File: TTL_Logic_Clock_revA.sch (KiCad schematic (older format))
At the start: 93 parts, among them J1 PJ-202A, J2 Conn_01x04_Female, U1 SN74HC74N, U10 SN74LS47N, U11 SN74LS190N, U12 SN74LS47N, U13 SN74LS47N, U14 SN74LS47N, U15 SN74LS47N, U2 SN74HC00N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

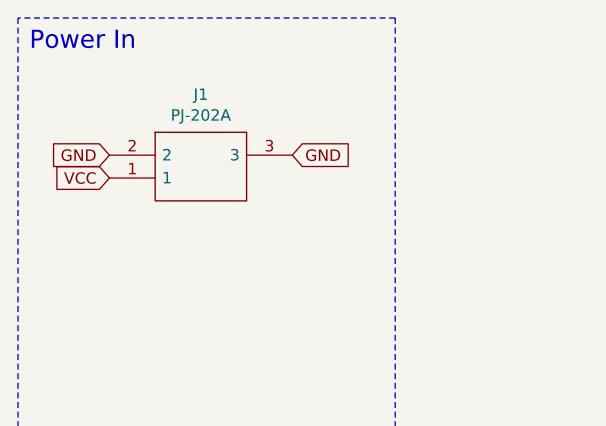
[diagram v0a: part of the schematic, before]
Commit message: Revert "new updates"
This reverts commit 53f30aa524d5c5c52be93e0d1f9b706b91b0ddee.
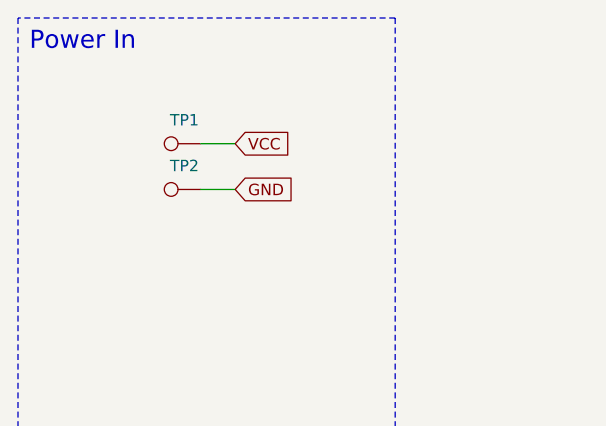
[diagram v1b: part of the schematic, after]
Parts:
- removed J1: PJ-202A, harit-connectors-dc:CUI_PJ-202A, symbol harit-connectors-dc:PJ-202A
- added TP1, TP2: TestPoint, TestPoint:TestPoint_Keystone_5015_Micro-Minature, symbol Connector:TestPoint
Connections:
- net GND: now also TP2.1
- net VCC: now also TP1.1
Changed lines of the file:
@@
 	1    0    0    -1
 $EndComp
-Text GLabel 950  1250 0    50   Input ~ 0
-VCC
-Text GLabel 1750 1150 2    50   Input ~ 0
+Text GLabel 1500 1100 2    50   Input ~ 0
+VCC
+Wire Wire Line
+	1350 1100 1500 1100
+Text GLabel 1500 1300 2    50   Input ~ 0
 GND
+Wire Wire Line
+	1350 1300 1500 1300
 $Comp
 L SparkFun-Capacitors:0.1UF-0402-16V-10% C1
@@
 Text GLabel 21150 1600 2    50   Input ~ 0
 VCC
+$Comp
+L Connector:TestPoint TP1
+U 1 1 6034A17C
+P 1350 1100
+F 0 "TP1" V 1453 1172 50  0000 C CNN
+F 1 "TestPoint" V 1454 1172 50  0001 C CNN
+F 2 "TestPoint:TestPoint_Keystone_5015_Micro-Minature" H 1550 1100 50  0001 C CNN
+F 3 "~" H 1550 1100 50  0001 C CNN
+	1    1350 1100
+	0    -1   -1   0
+$EndComp
+$Comp
+L Connector:TestPoint TP2
+U 1 1 603535D8
+P 1350 1300
+F 0 "TP2" V 1453 1372 50  0000 C CNN
+F 1 "TestPoint" V 1454 1372 50  0001 C CNN
+F 2 "TestPoint:TestPoint_Keystone_5015_Micro-Minature" H 1550 1300 50  0001 C CNN
+F 3 "~" H 1550 1300 50  0001 C CNN
+	1    1350 1300
+	0    -1   -1   0
+$EndComp
 Text GLabel 20100 7200 0    50   Input ~ 0
 1Hz
@@
 Wire Wire Line
 	3500 5250 3650 5250
-$Comp
-L harit-connectors-dc:PJ-202A J1
-U 1 1 60180FA8
-P 950 1150
-F 0 "J1" H 1350 1415 50  0000 C CNN
-F 1 "PJ-202A" H 1350 1324 50  0000 C CNN
-F 2 "harit-connectors-dc:CUI_PJ-202A" H 1600 1250 50  0001 L CNN
-F 3 "https://www.cuidevices.com/product/resource/pj-202a.pdf" H 1600 1150 50  0001 L CNN
-F 4 "DC Power Connectors Power Jacks" H 1600 1050 50  0001 L CNN "Description"
-F 5 "11.2" H 1600 950 50  0001 L CNN "Height"
-F 6 "490-PJ-202A" H 1600 850 50  0001 L CNN "Mouser Part Number"
-F 7 "https://www.mouser.co.uk/ProductDetail/CUI-Devices/PJ-202A?qs=WyjlAZoYn50aq4XmSpZ3Rg%3D%3D" H 1600 750 50  0001 L CNN "Mouser Price/Stock"
-F 8 "CUI Inc." H 1600 650 50  0001 L CNN "Manufacturer_Name"
-F 9 "PJ-202A" H 1600 550 50  0001 L CNN "Manufacturer_Part_Number"
-	1    950  1150
-	1    0    0    -1
-$EndComp
-Text GLabel 950  1150 0    50   Input ~ 0
-GND
 $EndSCHEMATC
